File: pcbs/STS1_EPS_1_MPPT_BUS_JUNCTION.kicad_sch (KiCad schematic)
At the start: 15 parts, among them Q2 SI7135DP-T1-GE3, Q3 SI7135DP-T1-GE3, U11 TMCS1101A3B-Q1, U19 TMCS1101A3B-Q1, U20 TMCS1101A3B-Q1, U21 TMCS1101A3B-Q1, U22 TMCS1101A3B-Q1, U23 TMCS1101A3B-Q1, U24 TMCS1101A3B-Q1, U25 TMCS1101A3B-Q1, U26 TMCS1101A3B-Q1

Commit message: Added testpoints to STS1_EPS_1.
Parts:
- added TP14, TP15: TestPoint, TestPoint:TestPoint_THTPad_D1.0mm_Drill0.5mm, symbol Connector:TestPoint
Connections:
- net DS1_SIGNAL: now also TP14.1
- net DS2_SIGNAL: now also TP15.1
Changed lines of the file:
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@@
   (junction (at 181.61 43.18) (diameter 0) (color 0 0 0 0)
   )
+  (junction (at 213.36 57.15) (diameter 0) (color 0 0 0 0)
+  )
   (junction (at 257.81 43.18) (diameter 0) (color 0 0 0 0)
   )
@@
   (junction (at 245.11 53.34) (diameter 0) (color 0 0 0 0)
   )
+  (junction (at 245.11 57.15) (diameter 0) (color 0 0 0 0)
+  )
   (junction (at 207.01 43.18) (diameter 0) (color 0 0 0 0)
   )
@@
     (stroke (width 0) (type default) (color 0 0 0 0))
   )
-  (wire (pts (xy 245.11 53.34) (xy 245.11 59.69))
+  (wire (pts (xy 245.11 53.34) (xy 245.11 57.15))
     (stroke (width 0) (type default) (color 0 0 0 0))
   )
@@
     (stroke (width 0) (type default) (color 0 0 0 0))
   )
-  (wire (pts (xy 213.36 53.34) (xy 213.36 59.69))
+  (wire (pts (xy 213.36 53.34) (xy 213.36 57.15))
     (stroke (width 0) (type default) (color 0 0 0 0))
   )
   (wire (pts (xy 229.87 43.18) (xy 238.76 43.18))
+    (stroke (width 0) (type default) (color 0 0 0 0))
+  )
+  (wire (pts (xy 245.11 57.15) (xy 245.11 59.69))
+    (stroke (width 0) (type default) (color 0 0 0 0))
+  )
+  (wire (pts (xy 213.36 57.15) (xy 213.36 59.69))
     (stroke (width 0) (type default) (color 0 0 0 0))
   )
@@
     (pin "6")
     (pin "7")
+  )
+  (symbol (lib_id "Connector:TestPoint") (at 245.11 57.15 270) (unit 1)
+    (in_bom yes) (on_board yes) (fields_autoplaced)
+    (property "Reference" "TP15" (id 0) (at 250.825 55.8799 90)
+      (effects (font (size 1.27 1.27)) (justify left))
+    )
+    (property "Value" "TestPoint" (id 1) (at 250.825 58.4199 90)
+      (effects (font (size 1.27 1.27)) (justify left))
+    )
+    (property "Footprint" "TestPoint:TestPoint_THTPad_D1.0mm_Drill0.5mm" (id 2) (at 245.11 62.23 0)
+      (effects (font (size 1.27 1.27)) hide)
+    )
+    (property "Datasheet" "~" (id 3) (at 245.11 62.23 0)
+      (effects (font (size 1.27 1.27)) hide)
+    )
+    (pin "1")
   )
   (symbol (lib_id "power:GND") (at 124.46 41.91 0) (unit 1)
@@
       (effects (font (size 1.27 1.27)) hide)
     )
+    (pin "1")
+  )
+  (symbol (lib_id "Connector:TestPoint") (at 213.36 57.15 270) (unit 1)
+    (in_bom yes) (on_board yes) (fields_autoplaced)
+    (property "Reference" "TP14" (id 0) (at 219.075 55.8799 90)
+      (effects (font (size 1.27 1.27)) (justify left))
+    )
+    (property "Value" "TestPoint" (id 1) (at 219.075 58.4199 90)
+      (effects (font (size 1.27 1.27)) (justify left))
+    )
+    (property "Footprint" "TestPoint:TestPoint_THTPad_D1.0mm_Drill0.5mm" (id 2) (at 213.36 62.23 0)
+      (effects (font (size 1.27 1.27)) hide)
+    )
+    (property "Datasheet" "~" (id 3) (at 213.36 62.23 0)
+      (effects (font (size 1.27 1.27)) hide)
+    )

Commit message: worked on sts1_eps_1
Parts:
- removed U11, U19, U20, U21, U22, U23, U24, U25, U26: TMCS1101A3B-Q1, Package_SO:SOIC-8_3.9x4.9mm_P1.27mm, symbol STS_Sensor_Current:TMCS1101Q1
- added R21, R22, R23, R39, R40, R41, R42, R43: 50m, Resistor_SMD:R_0805_2012Metric, symbol Device:R
- added R44: 10m, Resistor_SMD:R_0805_2012Metric, symbol Device:R
- added U11: INA180A4, Package_TO_SOT_SMD:SOT-23-5, symbol STS_Sensor_Current:INA180A4
- added U13, U4: INA4180A4, Package_SO:TSSOP-14_4.4x5mm_P0.65mm, symbol STS_Sensor_Current:INA4180A4
- added U19: TPS259472ARPW, STS_Package_DFN_QFN:TPS259472ARPWR, symbol STS_Power_Management:TPS259472ARPW
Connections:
- net 5V: now also U11.5 (VS), U13.4 (VS), U4.4 (VS)
- net GND: now also U11.2 (GND), U13.11 (GND), U4.11 (GND)
- net MPPT_I_SUM: now also U11.1 (OUT)
- net MPPT_X+_1_I: now also U4.1 (OUT1)
- net MPPT_X+_1_IN: now also R21.2, U4.3 (IN+1)
- net MPPT_X+_2_I: now also U4.7 (OUT2)
- net MPPT_X+_2_IN: now also R22.2, U4.5 (IN+2)
- net MPPT_X-_1_I: now also U4.8 (OUT3)
- net MPPT_X-_1_IN: now also R23.2, U4.10 (IN+3)
- net MPPT_X-_2_I: now also U4.14 (OUT4)
- net MPPT_X-_2_IN: now also R39.2, U4.12 (IN+4)
- net MPPT_Y+_1_I: now also U13.1 (OUT1)
- net MPPT_Y+_1_IN: now also R40.2, U13.3 (IN+1)
- net MPPT_Y-_1_I: now also U13.7 (OUT2)
- net MPPT_Y-_1_IN: now also R41.2, U13.5 (IN+2)
- net MPPT_Z+_1_I: now also U13.8 (OUT3)
- net MPPT_Z+_1_IN: now also R42.2, U13.10 (IN+3)
- net MPPT_Z+_2_I: now also U13.14 (OUT4)
- net MPPT_Z+_2_IN: now also R43.2, U13.12 (IN+4)
- net at Q2.1, Q2.2, Q2.3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: now also R44.1, U11.4 (IN-)
- new net: R21.1, R22.1, R23.1, R39.1, R40.1, R41.1, R42.1, R43.1, R44.2, U11.3 (IN+), U13.13 (IN-4), U13.2 (IN-1), U13.6 (IN-2), U13.9 (IN-3), U4.13 (IN-4), U4.2 (IN-1), U4.6 (IN-2), U4.9 (IN-3)

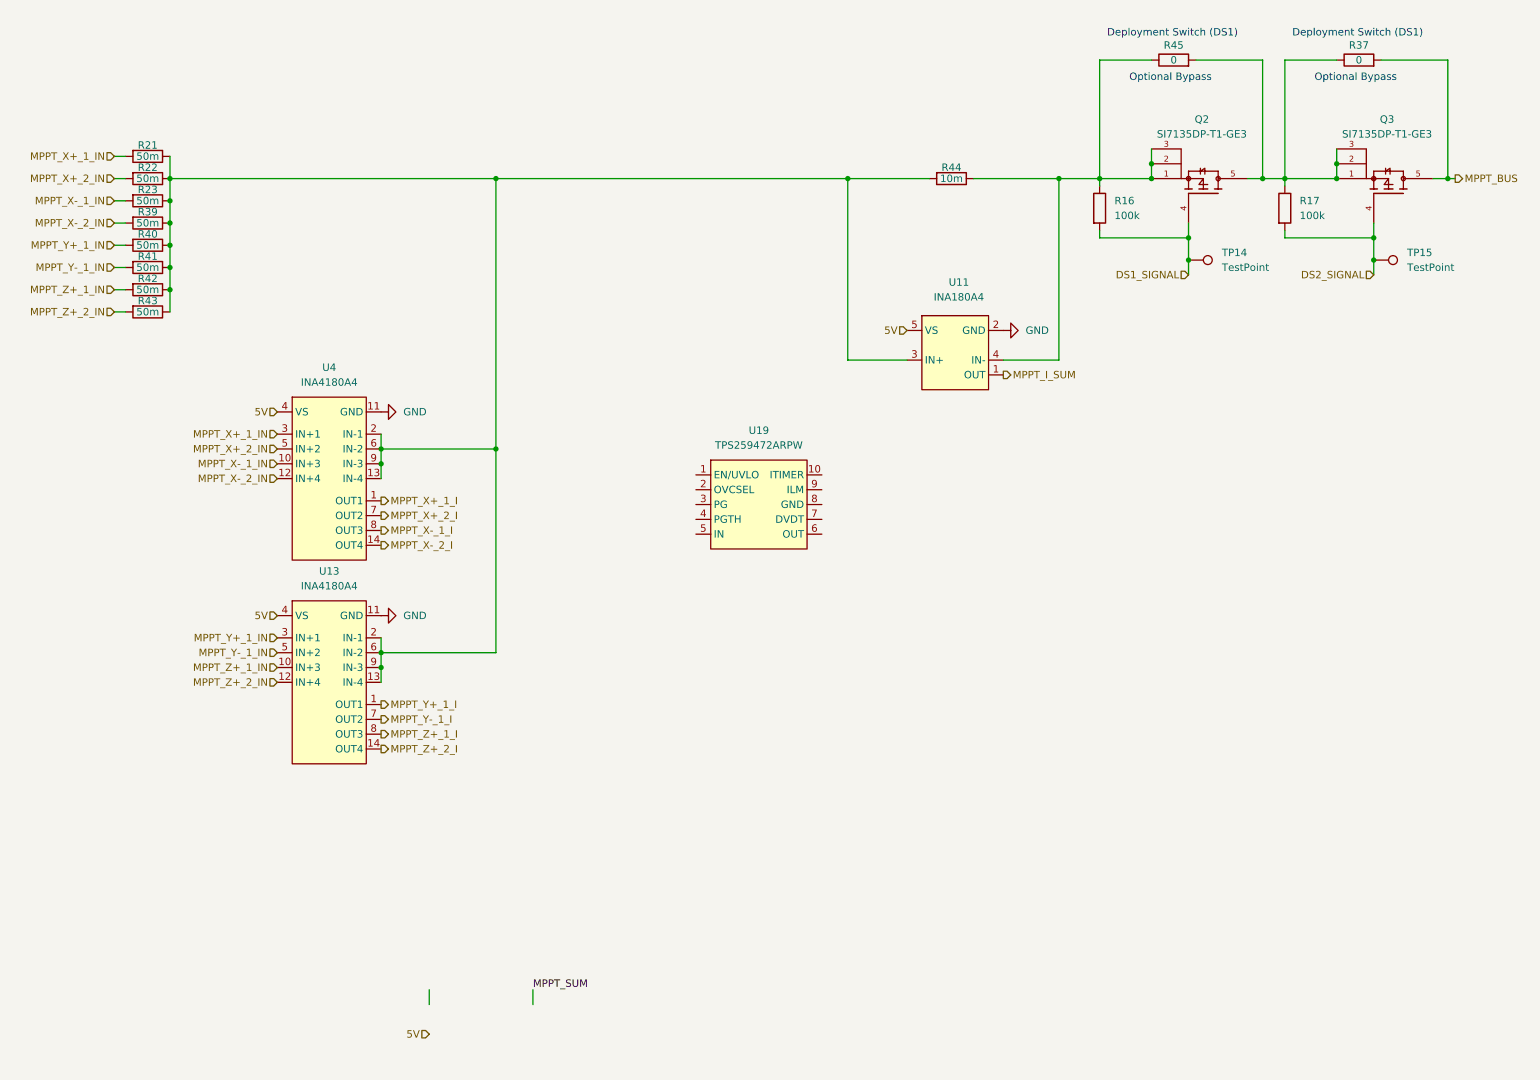
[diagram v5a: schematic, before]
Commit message: Worked on STS1_EPS_1.
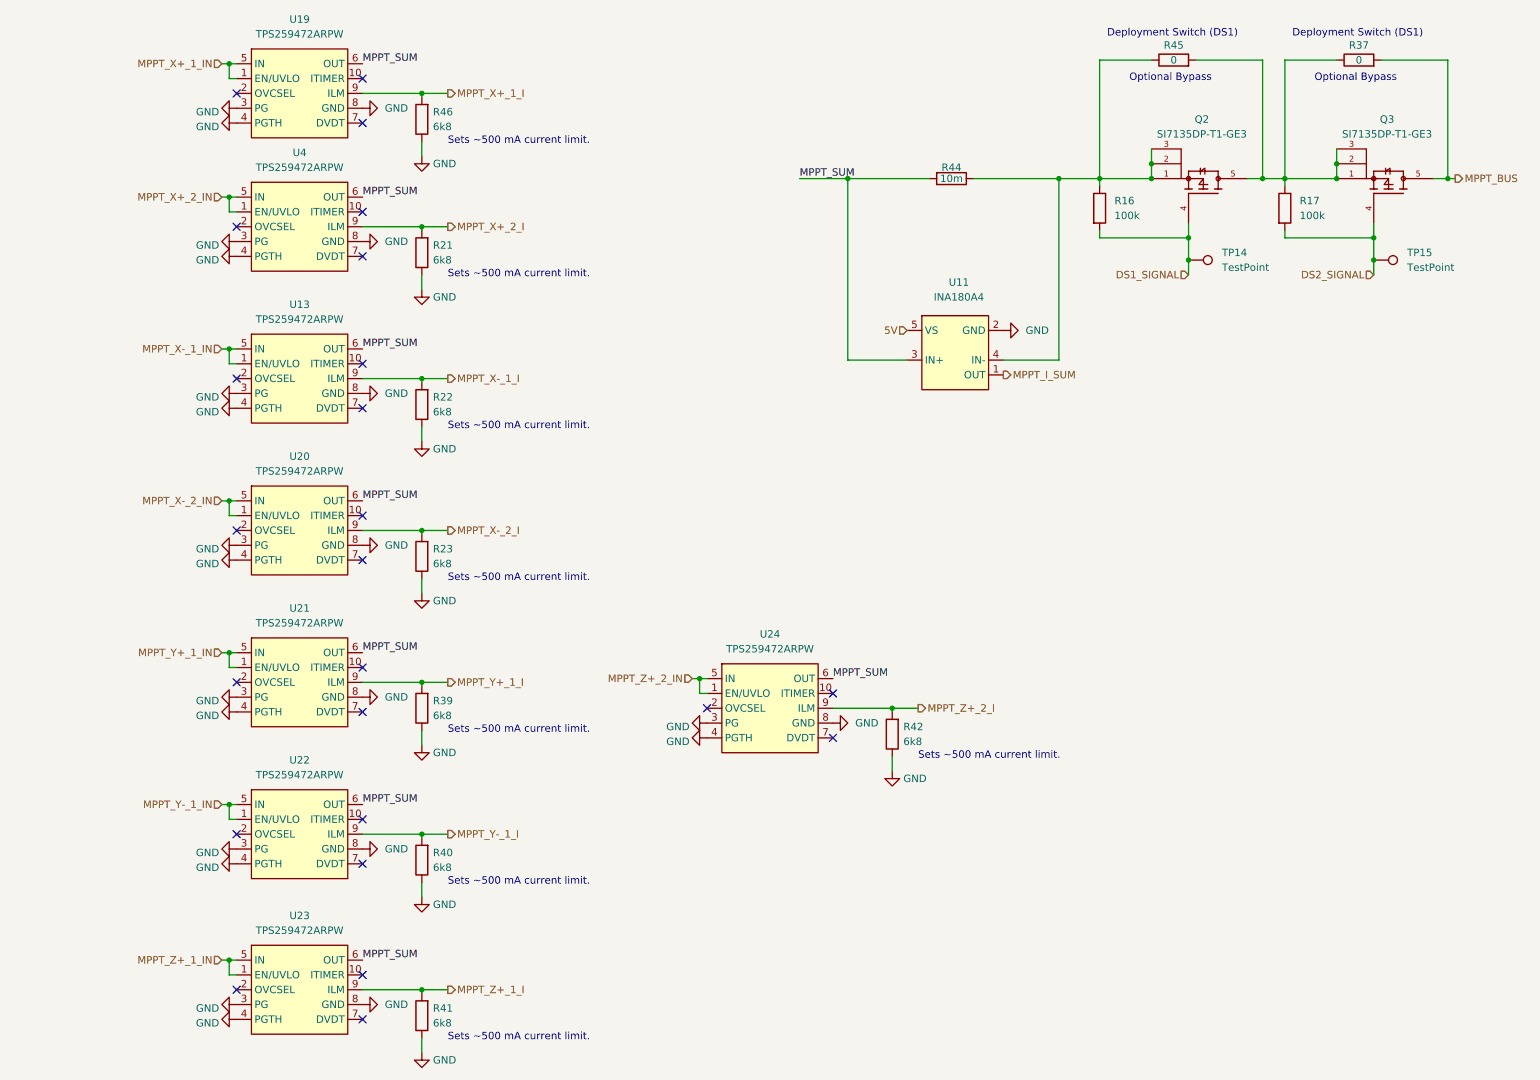
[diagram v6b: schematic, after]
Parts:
- removed R43: 50m, Resistor_SMD:R_0805_2012Metric, symbol Device:R
- removed U13, U4: INA4180A4, Package_SO:TSSOP-14_4.4x5mm_P0.65mm, symbol STS_Sensor_Current:INA4180A4
- added R46: 6k8, Resistor_SMD:R_0805_2012Metric, symbol Device:R
- added U13, U20, U21, U22, U23, U24, U4: TPS259472ARPW, STS_Package_DFN_QFN:TPS259472ARPWR, symbol STS_Power_Management:TPS259472ARPW
- Q2, Q3: footprint STS_Package_SO:POWERPAK_SO8_single -> TRANS_SI7135DP-T1-GE3
- R21, R22, R23, R39, R40, R41, R42: value 50m -> 6k8
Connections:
- net GND: now also R21.1, R22.1, R23.1, R39.1, R40.1, R41.1, R42.1, U19.3 (PG), U19.4 (PGTH), U19.8 (GND), R46.1, U13.3 (PG), U13.4 (PGTH), U13.8 (GND), U20.3 (PG), U20.4 (PGTH), U20.8 (GND), U21.3 (PG), U21.4 (PGTH), U21.8 (GND), U22.3 (PG), U22.4 (PGTH), U22.8 (GND), U23.3 (PG), U23.4 (PGTH), U23.8 (GND), U24.3 (PG), U24.4 (PGTH), U24.8 (GND), U4.3 (PG), U4.4 (PGTH), U4.8 (GND)
- net MPPT_SUM: now also R44.2, U11.3 (IN+), U19.6 (OUT), U13.6 (OUT), U20.6 (OUT), U21.6 (OUT), U22.6 (OUT), U23.6 (OUT), U24.6 (OUT), U4.6 (OUT)
- net MPPT_X+_1_I: now also U19.9 (ILM), R46.2
- net MPPT_X+_1_IN: now also U19.1 (EN/UVLO), U19.5 (IN); no longer R21.2
- net MPPT_X+_2_I: now also R21.2, U4.9 (ILM)
- net MPPT_X+_2_IN: now also U4.1 (EN/UVLO), U4.5 (IN); no longer R22.2
- net MPPT_X-_1_I: now also R22.2, U13.9 (ILM)
- net MPPT_X-_1_IN: now also U13.1 (EN/UVLO), U13.5 (IN); no longer R23.2
- net MPPT_X-_2_I: now also R23.2, U20.9 (ILM)
- net MPPT_X-_2_IN: now also U20.1 (EN/UVLO), U20.5 (IN); no longer R39.2
- net MPPT_Y+_1_I: now also R39.2, U21.9 (ILM)
- net MPPT_Y+_1_IN: now also U21.1 (EN/UVLO), U21.5 (IN); no longer R40.2
- net MPPT_Y-_1_I: now also R40.2, U22.9 (ILM)
- net MPPT_Y-_1_IN: now also U22.1 (EN/UVLO), U22.5 (IN); no longer R41.2
- net MPPT_Z+_1_I: now also R41.2, U23.9 (ILM)
- net MPPT_Z+_1_IN: now also U23.1 (EN/UVLO), U23.5 (IN); no longer R42.2
- net MPPT_Z+_2_I: now also R42.2, U24.9 (ILM)
- net MPPT_Z+_2_IN: now also U24.1 (EN/UVLO), U24.5 (IN)
- no-connect marks 0 -> 24
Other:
- note added: "Sets ~500 mA current limit."
- moved on the sheet: U19

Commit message: Worked on STS1_EPS_1.
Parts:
- Q2, Q3: footprint TRANS_SI7135DP-T1-GE3 -> STS_Package_SO:POWERPAK_SO8_single
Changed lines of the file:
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@@
     (pin "2")
   )
-  (symbol (lib_name "TPS259472ARPW_6") (lib_id "STS_Power_Management:TPS259472ARPW") (at 59.055 161.925 0) (unit 1)
+  (symbol (lib_id "STS_Power_Management:TPS259472ARPW") (at 59.055 161.925 0) (unit 1)
     (in_bom yes) (on_board yes) (fields_autoplaced)
     (property "Reference" "U22" (id 0) (at 60.96 142.875 0))
@@
     (property "Reference" "Q3" (id 0) (at 247.396 33.02 90))
     (property "Value" "SI7135DP-T1-GE3" (id 1) (at 247.396 35.56 90))
-    (property "Footprint" "TRANS_SI7135DP-T1-GE3" (id 2) (at 252.73 40.64 0)
+    (property "Footprint" "STS_Package_SO:POWERPAK_SO8_single" (id 2) (at 252.73 40.64 0)
       (effects (font (size 1.27 1.27)) (justify left bottom) hide)
     )
@@
     (pin "5")
   )
-  (symbol (lib_name "TPS259472ARPW_3") (lib_id "STS_Power_Management:TPS259472ARPW") (at 59.055 34.925 0) (unit 1)
+  (symbol (lib_id "STS_Power_Management:TPS259472ARPW") (at 59.055 34.925 0) (unit 1)
     (in_bom yes) (on_board yes) (fields_autoplaced)
     (property "Reference" "U19" (id 0) (at 60.96 15.875 0))
@@
     (pin "9")
   )
-  (symbol (lib_name "TPS259472ARPW_5") (lib_id "STS_Power_Management:TPS259472ARPW") (at 59.055 83.82 0) (unit 1)
+  (symbol (lib_id "STS_Power_Management:TPS259472ARPW") (at 59.055 83.82 0) (unit 1)
     (in_bom yes) (on_board yes) (fields_autoplaced)
     (property "Reference" "U13" (id 0) (at 60.96 64.77 0))
@@
     (pin "2")
   )
-  (symbol (lib_name "TPS259472ARPW_1") (lib_id "STS_Power_Management:TPS259472ARPW") (at 139.7 140.335 0) (unit 1)
+  (symbol (lib_id "STS_Power_Management:TPS259472ARPW") (at 139.7 140.335 0) (unit 1)
     (in_bom yes) (on_board yes) (fields_autoplaced)
     (property "Reference" "U24" (id 0) (at 141.605 121.285 0))
@@
     (pin "1")
   )
-  (symbol (lib_name "TPS259472ARPW_7") (lib_id "STS_Power_Management:TPS259472ARPW") (at 59.055 135.89 0) (unit 1)
+  (symbol (lib_id "STS_Power_Management:TPS259472ARPW") (at 59.055 135.89 0) (unit 1)
     (in_bom yes) (on_board yes) (fields_autoplaced)
     (property "Reference" "U21" (id 0) (at 60.96 116.84 0))
@@
     (pin "1")
   )
-  (symbol (lib_name "TPS259472ARPW_4") (lib_id "STS_Power_Management:TPS259472ARPW") (at 59.055 109.855 0) (unit 1)
+  (symbol (lib_id "STS_Power_Management:TPS259472ARPW") (at 59.055 109.855 0) (unit 1)
     (in_bom yes) (on_board yes) (fields_autoplaced)
     (property "Reference" "U20" (id 0) (at 60.96 90.805 0))
@@
     (property "Reference" "Q2" (id 0) (at 215.646 33.02 90))
     (property "Value" "SI7135DP-T1-GE3" (id 1) (at 215.646 35.56 90))
-    (property "Footprint" "TRANS_SI7135DP-T1-GE3" (id 2) (at 220.98 40.64 0)
+    (property "Footprint" "STS_Package_SO:POWERPAK_SO8_single" (id 2) (at 220.98 40.64 0)
       (effects (font (size 1.27 1.27)) (justify left bottom) hide)
     )
@@
     (pin "1")
   )
-  (symbol (lib_name "TPS259472ARPW_2") (lib_id "STS_Power_Management:TPS259472ARPW") (at 59.055 57.785 0) (unit 1)
+  (symbol (lib_id "STS_Power_Management:TPS259472ARPW") (at 59.055 57.785 0) (unit 1)
     (in_bom yes) (on_board yes) (fields_autoplaced)
     (property "Reference" "U4" (id 0) (at 60.96 38.735 0))
